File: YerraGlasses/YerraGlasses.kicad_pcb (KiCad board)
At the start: 4 copper layers, 68 x 21.5 mm, 28 parts, among them J1 Conn_01x02_Pin, J11 USB_C_Receptacle_USB2.0_16P, J2 Conn_01x02_Pin, J3 Conn_01x02_Pin, J4 Conn_01x02_Pin, SW1 SW_SPDT, U1 ESP32-S3-WROOM-1, U2 MAX98357A, U3 MAX98357A, U4 RT9013-33GB

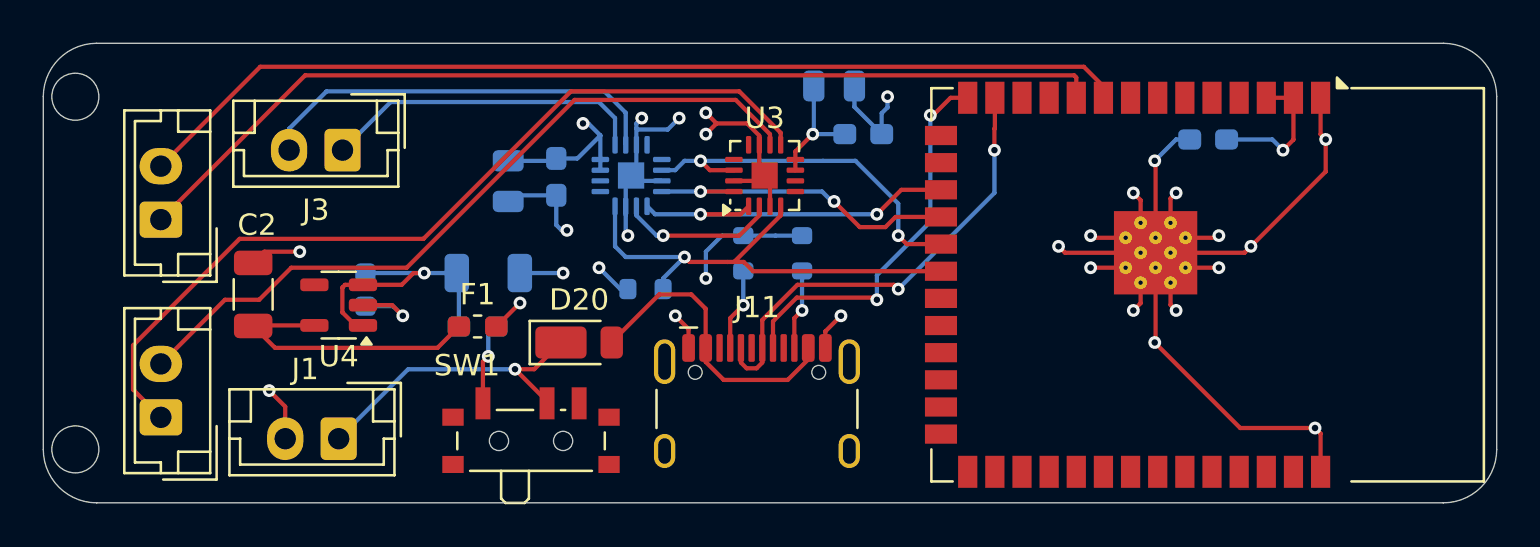
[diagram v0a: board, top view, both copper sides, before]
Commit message: added power connector, updated cad
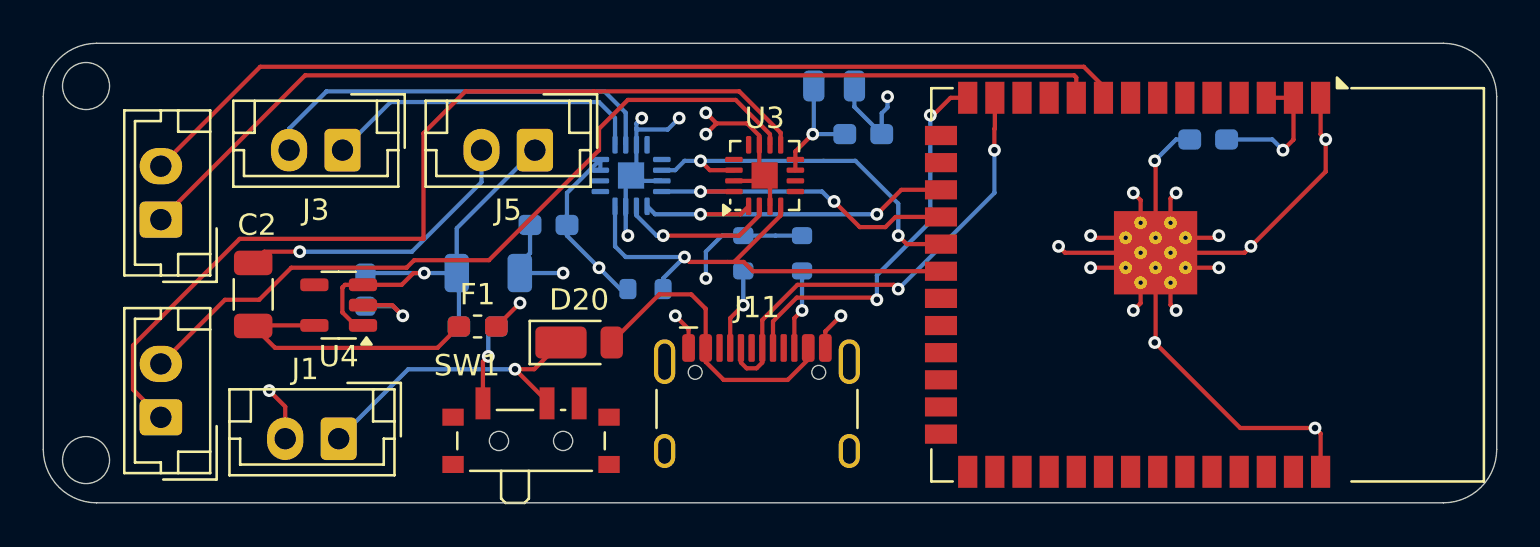
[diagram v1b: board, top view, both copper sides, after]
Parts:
- removed C4: 10u, Capacitor_SMD:C_0805_2012Metric
- removed the REF** at (165.5, 60.0)
- removed the REF** at (165.5, 43.5)
- added J5: Conn_01x02_Pin, Connector_JST:JST_EH_B2B-EH-A_1x02_P2.50mm_Vertical, F.Cu at (187.0, 46.0)
- added REF**: MountingHole_2.2mm_M2_custom, MountingHole:MountingHole_2.2mm_M2_custom, F.Cu at (166.0, 43.0)
- added REF**: MountingHole_2.2mm_M2_custom, MountingHole:MountingHole_2.2mm_M2_custom, F.Cu at (166.0, 60.5)
- moved C3 2.28 mm to (187.6, 49.5), turned to 0 degrees
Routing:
- net GND: track 98.0 -> 107.4 mm, vias 28 -> 27
- net +5V: track 13.5 -> 20.7 mm
- net /Connectors/OUTP_2: track 40.5 -> 43.4 mm
- net +3V3: track 31.0 -> 30.3 mm, vias 6 -> 5
- net /Connectors/OUTN_2: track 34.8 -> 35.4 mm
